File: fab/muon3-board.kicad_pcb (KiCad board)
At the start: 4 copper layers, 160 x 120 mm, 106 parts

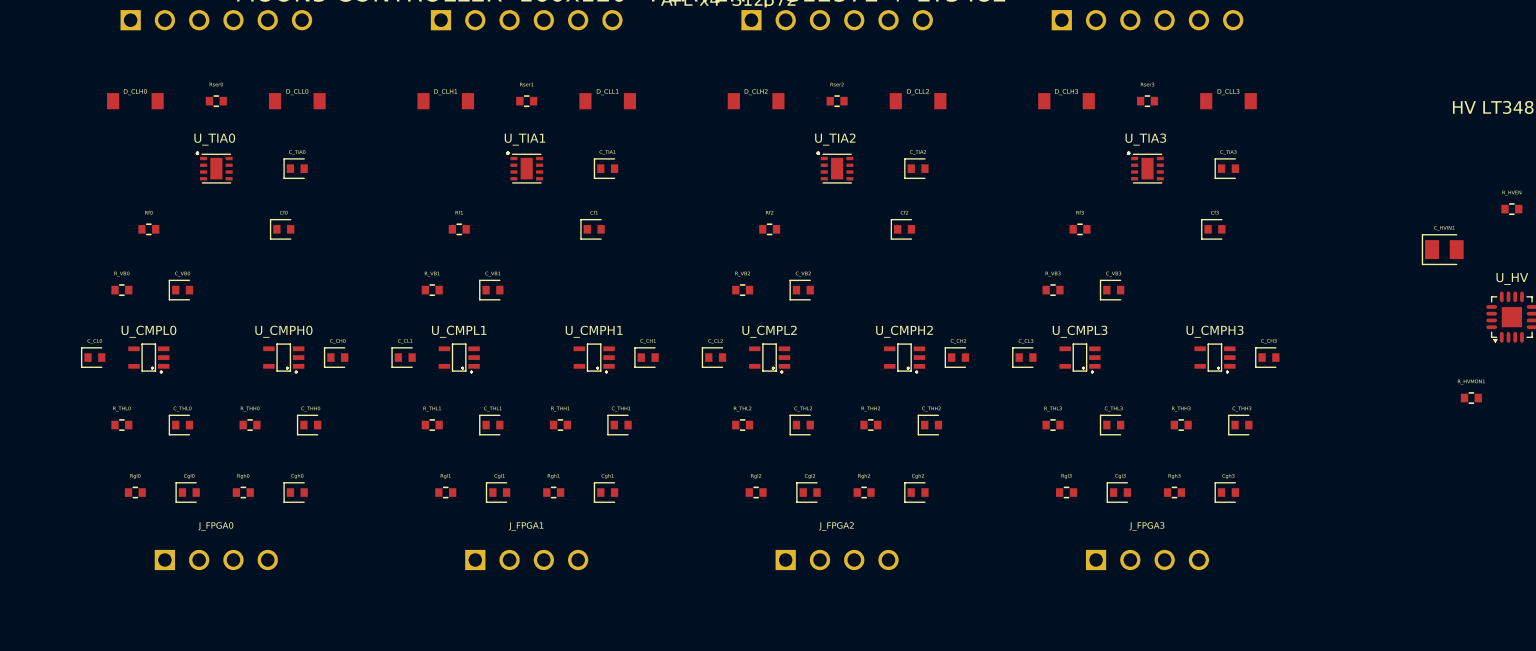
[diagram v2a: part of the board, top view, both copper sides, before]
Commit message: board: datasheet-driven AFE/HV placement (RF/noise/high-speed)
Optimize the placed front-end from vendor layout guidance.

OPA858 TIA (TI SLOS879):
- 10 Ω series R moved directly to the IN− pin (damp bond-wire/stray-C
  resonance) instead of up by the connector.
- VS decoupling (C_TIA) tight to VS_POS; Rf/Cf kept on the FB pin (min
  feedback parasitics) and close to FB/IN−.
- No-pour <keepout> under IN−/OUT/FB on top + L2 reference plane to strip
  summing-node parasitic capacitance (one per channel).
- Off-board SiPM (50 cm cable, fixed) → minimize the on-board connector→
  TIA path; cable modeled in cable_50cm.cir.

TLV3601: VCC decoupling tightened to the pin.

LT3482 HV (ADI 3482fa):
- Add mandatory 20 Ω series R at the APD pin (prevents APD-pin ring-below-
  ground damage on a short).

RF (nRF9151): guidance recorded for when the module is placed — 50 Ω U.FL
edge-launch direct to ANT (single shared LTE+GNSS, no matching), RF trace
on L2 with GND keepout, antenna keepout cylinder.

DRC-clean, zero overlaps. LAYOUT.md updated with the datasheet rationale.

Co-Authored-By: Claude Opus 4.8 <noreply@anthropic.com>
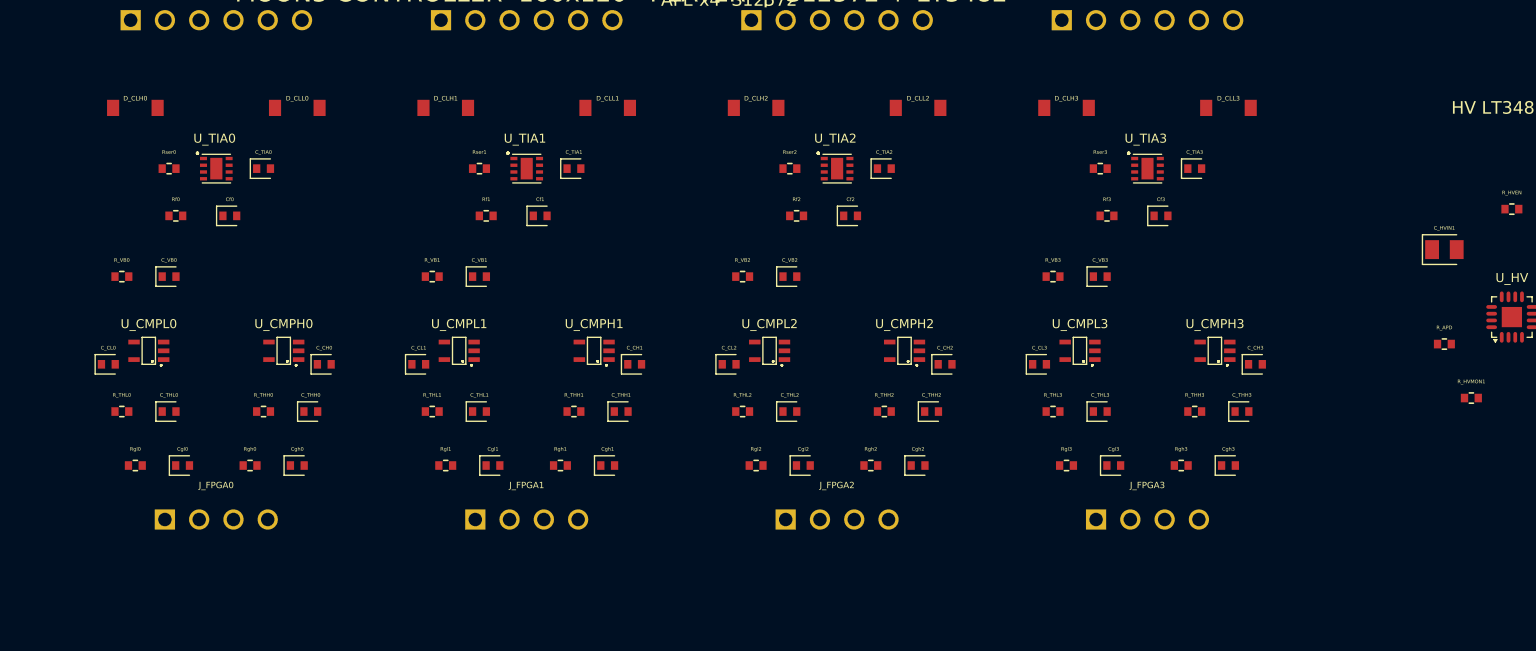
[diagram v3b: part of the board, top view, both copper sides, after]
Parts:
- added R_APD: 20Ω, tscircuit:resistor_res0402, F.Cu at (161.0, 70.0)
- moved Rser0 6.10 mm to (66.5, 57.0)
- moved Rser1 6.10 mm to (89.5, 57.0)
- moved Rser2 6.10 mm to (112.5, 57.0)
- moved Rser3 6.10 mm to (135.5, 57.0)
- moved Cf0 4.12 mm to (71.0, 60.5)
- moved Cf1 4.12 mm to (94.0, 60.5)
- moved Cf2 4.12 mm to (117.0, 60.5)
- moved Cf3 4.12 mm to (140.0, 60.5)
- moved J_FPGA0 3.00 mm to (70.0, 83.0)
- moved J_FPGA1 3.00 mm to (93.0, 83.0)
- moved J_FPGA2 3.00 mm to (116.0, 83.0)
- moved J_FPGA3 3.00 mm to (139.0, 83.0)
- moved C_TIA0 2.50 mm to (73.5, 57.0)
- moved C_TIA1 2.50 mm to (96.5, 57.0)
- moved C_TIA2 2.50 mm to (119.5, 57.0)
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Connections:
- U_HV pad 2: HV_BIAS -> HV_APD

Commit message: board: complete decoupling + rail reservoirs for placed ICs
Add the required passives for the currently-placed subsystems (AFE x4,
HV); per-IC passives for the not-yet-placed digital/TEC/power ICs go in
with those ICs (their pins define the nets).

- OPA858: add per-channel 2.2uF local bulk (C_TIAB) alongside the 0.1uF
  at VS+ (TI SLOS879 layout: 0.1uF + 2.2uF).
- board/rails.tsx: distributed bulk reservoirs on the rails the placed
  parts draw from — VANA 5V (2x10uF+100nF, feeds 4x OPA858), VDIG 3.3V
  (2x10uF+100nF, feeds 8x TLV3601), V12 (22uF+10uF+100nF, feeds LT3482
  and later TEC/fans) — placed at the DIGITAL-zone distribution point.

Already present and audited: TLV3601 0.1uF per comparator; LT3482 input
10uF+100nF, HV_EN pull-up, APD 20 ohm, HV_MON divider.

Deferred (with their ICs): nRF9151/iCE40/RP2040/flash/DAC/ADC/BME280/
CH224K/DRV8873 per-pin decoupling; I2C/reset/boot/config pull-ups;
regulator in/out caps; V1V2 core reservoir.

116 components (41 caps), DRC-clean, zero overlaps.

Co-Authored-By: Claude Opus 4.8 <noreply@anthropic.com>
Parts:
- added C_TIAB0: 2.2uF, tscircuit:capacitor_0603, F.Cu at (76.0, 59.0)
- added C_TIAB1: 2.2uF, tscircuit:capacitor_0603, F.Cu at (99.0, 59.0)
- added C_TIAB2: 2.2uF, tscircuit:capacitor_0603, F.Cu at (122.0, 59.0)
- added C_TIAB3: 2.2uF, tscircuit:capacitor_0603, F.Cu at (145.0, 59.0)
- added C_V12_1: 22uF, tscircuit:capacitor_1206, F.Cu at (114.0, 98.0)
- added C_V12_2: 10uF, tscircuit:capacitor_0805, F.Cu at (118.0, 98.0)
- added C_V12_3: 100nF, tscircuit:capacitor_0402, F.Cu at (121.5, 98.0)
- added C_VANA1: 10uF, tscircuit:capacitor_0805, F.Cu at (58.0, 96.0)
- added C_VANA2: 10uF, tscircuit:capacitor_0805, F.Cu at (62.0, 96.0)
- added C_VANA3: 100nF, tscircuit:capacitor_0402, F.Cu at (65.5, 96.0)
- added C_VDIG1: 10uF, tscircuit:capacitor_0805, F.Cu at (58.0, 101.0)
- added C_VDIG2: 10uF, tscircuit:capacitor_0805, F.Cu at (62.0, 101.0)
- added C_VDIG3: 100nF, tscircuit:capacitor_0402, F.Cu at (65.5, 101.0)

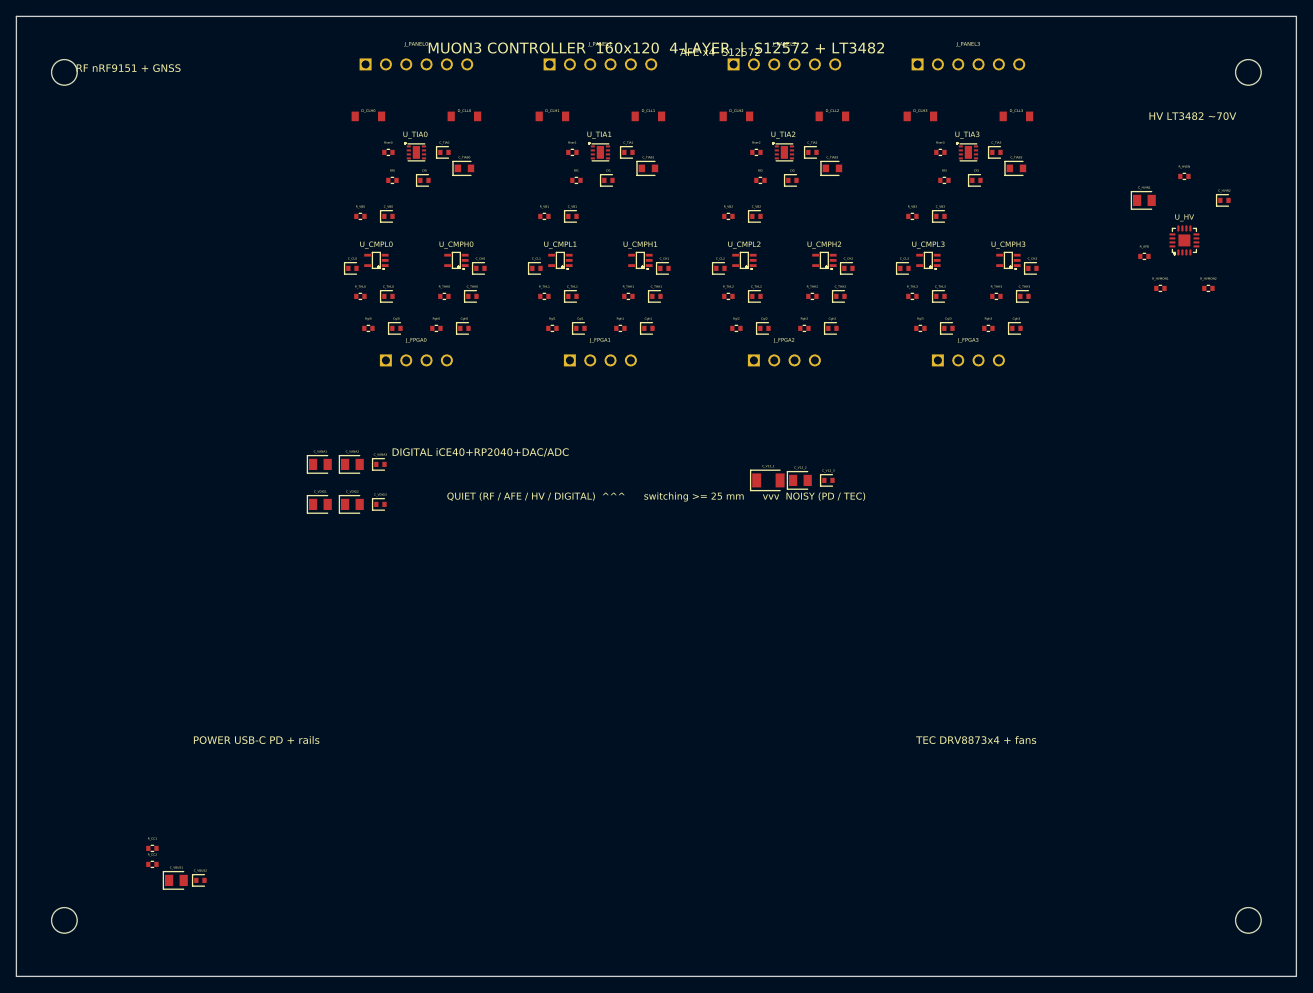
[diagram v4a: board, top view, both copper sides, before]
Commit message: board: populate POWER + RF, board now fully placed (230 components)
- power.tsx: USB-C receptacle (bottom edge, clear of corner hole) -> CH224K
  PD sink (CC pull-downs, CFG code stub for 12V, VDD decoupling, PG pull-up)
  -> TPS62933 3.3V buck with full network (in/out caps, 4.7uH inductor,
  BST/SS/RT, FB divider for 3.3V, EN pull-up).
- rf.tsx: nRF9151-LACA placed with VDD/VIO/VDD_GPIO, DEC0 cap, reset/enable
  pull-ups, supply decoupling; ANT -> U.FL edge-launch (single shared
  LTE+GNSS, 50 ohm, no matching, per Nordic). Import aliased (lowercase
  export name reads as an intrinsic JSX element otherwise).

Whole board: RF | AFE x4 | HV over DIGITAL / POWER / TEC — 230 placements,
49 BOM line items, DRC-clean, zero overlaps.

Flagged for datasheet/routing passes: CH224K 12V CFG code, USB-C A/B pin
map, buck L/FB/RT values, nRF9151 full GND stitch + RF trace, DAC80508 BGA
ball map, LT3482 boost network, VANA/V1V2/VCORE regulators, SIM connector,
and all inter-IC signal buses + routing. README status updated.

Co-Authored-By: Claude Opus 4.8 <noreply@anthropic.com>
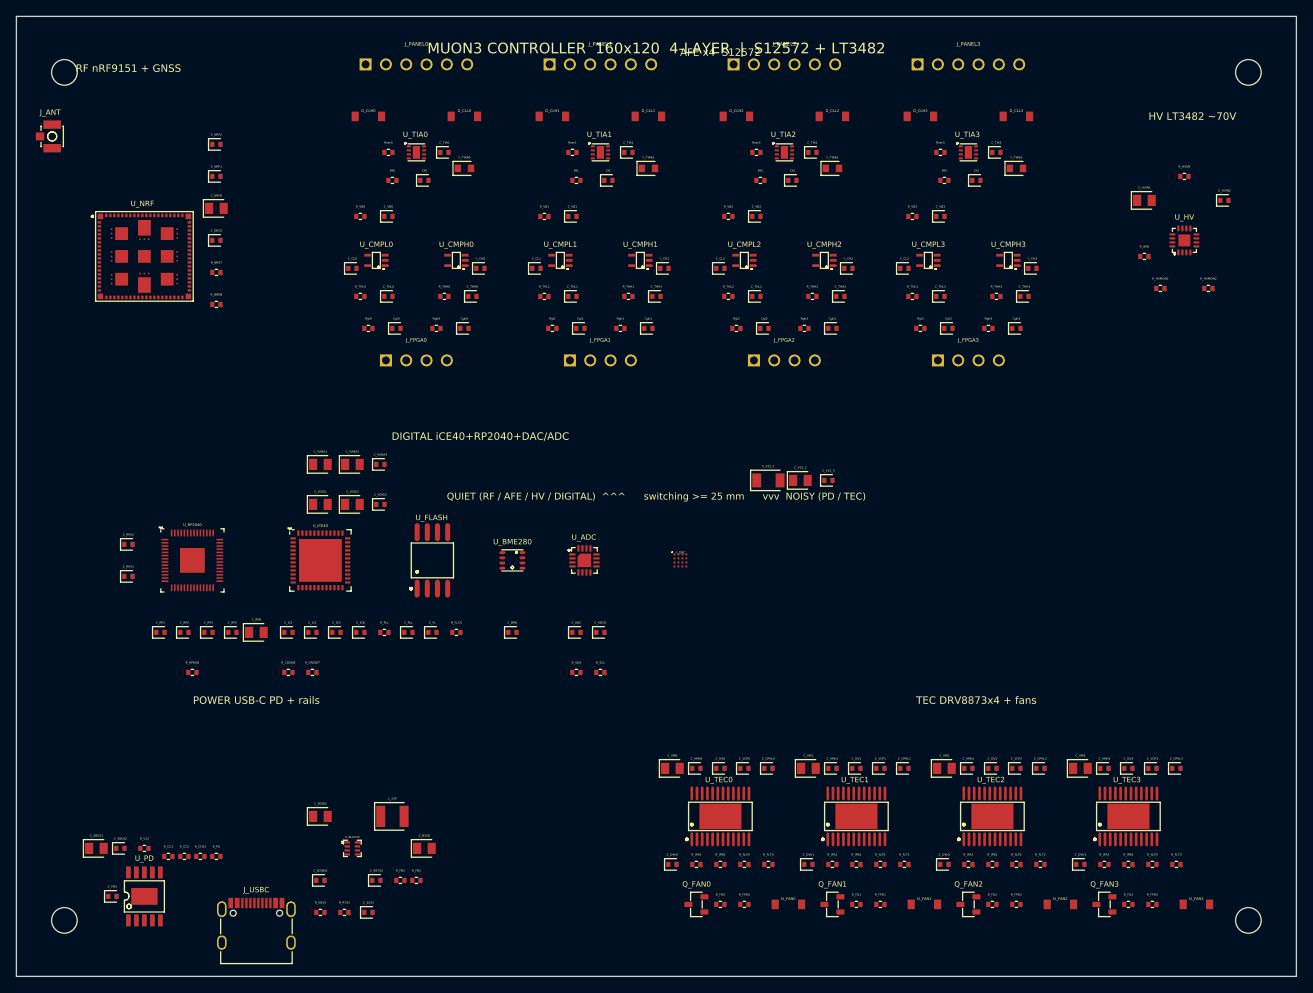
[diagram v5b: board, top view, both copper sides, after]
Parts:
- added C_ADC: 100nF, tscircuit:capacitor_0402, F.Cu at (90.0, 117.0)
- added C_ADCD: 1uF, tscircuit:capacitor_0402, F.Cu at (93.0, 117.0)
- added C_B33IN: 10uF, tscircuit:capacitor_0805, F.Cu at (58.0, 140.0)
- added C_B33IN2: 100nF, tscircuit:capacitor_0402, F.Cu at (58.0, 148.0)
- added C_B33O: 22uF, tscircuit:capacitor_0805, F.Cu at (71.0, 144.0)
- added C_BME: 100nF, tscircuit:capacitor_0402, F.Cu at (82.0, 117.0)
- added C_BST33: 100nF, tscircuit:capacitor_0402, F.Cu at (65.0, 148.0)
- added C_CPHL0: 47nF, tscircuit:capacitor_0402, F.Cu at (114.0, 134.0)
- added C_CPHL1: 47nF, tscircuit:capacitor_0402, F.Cu at (131.0, 134.0)
- added C_CPHL2: 47nF, tscircuit:capacitor_0402, F.Cu at (148.0, 134.0)
- added C_CPHL3: 47nF, tscircuit:capacitor_0402, F.Cu at (165.0, 134.0)
- added C_DEC0: 100nF, tscircuit:capacitor_0402, F.Cu at (45.0, 68.0)
- added C_DV0: 1uF, tscircuit:capacitor_0402, F.Cu at (108.0, 134.0)
- added C_DV1: 1uF, tscircuit:capacitor_0402, F.Cu at (125.0, 134.0)
- added C_DV2: 1uF, tscircuit:capacitor_0402, F.Cu at (142.0, 134.0)
- added C_DV3: 1uF, tscircuit:capacitor_0402, F.Cu at (159.0, 134.0)
- added C_DVh0: 100nF, tscircuit:capacitor_0402, F.Cu at (102.0, 146.0)
- added C_DVh1: 100nF, tscircuit:capacitor_0402, F.Cu at (119.0, 146.0)
- added C_DVh2: 100nF, tscircuit:capacitor_0402, F.Cu at (136.0, 146.0)
- added C_DVh3: 100nF, tscircuit:capacitor_0402, F.Cu at (153.0, 146.0)
- added C_FL: 100nF, tscircuit:capacitor_0402, F.Cu at (72.0, 117.0)
- added C_IC1: 100nF, tscircuit:capacitor_0402, F.Cu at (54.0, 117.0)
- added C_IC2: 100nF, tscircuit:capacitor_0402, F.Cu at (57.0, 117.0)
- added C_IC3: 100nF, tscircuit:capacitor_0402, F.Cu at (60.0, 117.0)
- added C_ICB: 1uF, tscircuit:capacitor_0402, F.Cu at (63.0, 117.0)
- added C_NRF1: 100nF, tscircuit:capacitor_0402, F.Cu at (45.0, 60.0)
- added C_NRF2: 100nF, tscircuit:capacitor_0402, F.Cu at (45.0, 56.0)
- added C_NRFB: 4.7uF, tscircuit:capacitor_0805, F.Cu at (45.0, 64.0)
- added C_PDV: 100nF, tscircuit:capacitor_0402, F.Cu at (32.0, 150.0)
- added C_PLL: 100nF, tscircuit:capacitor_0402, F.Cu at (69.0, 117.0)
- added C_RP1: 100nF, tscircuit:capacitor_0402, F.Cu at (38.0, 117.0)
- added C_RP2: 100nF, tscircuit:capacitor_0402, F.Cu at (41.0, 117.0)
- added C_RP3: 100nF, tscircuit:capacitor_0402, F.Cu at (44.0, 117.0)
- added C_RPB: 10uF, tscircuit:capacitor_0805, F.Cu at (50.0, 117.0)
- added C_RPV: 1uF, tscircuit:capacitor_0402, F.Cu at (47.0, 117.0)
- added C_RPX1: 18pF, tscircuit:capacitor_0402, F.Cu at (34.0, 110.0)
- added C_RPX2: 18pF, tscircuit:capacitor_0402, F.Cu at (34.0, 106.0)
- added C_SS33: 10nF, tscircuit:capacitor_0402, F.Cu at (64.0, 152.0)
- added C_VCP0: 1uF, tscircuit:capacitor_0402, F.Cu at (111.0, 134.0)
- added C_VCP1: 1uF, tscircuit:capacitor_0402, F.Cu at (128.0, 134.0)
- added C_VCP2: 1uF, tscircuit:capacitor_0402, F.Cu at (145.0, 134.0)
- added C_VCP3: 1uF, tscircuit:capacitor_0402, F.Cu at (162.0, 134.0)
- added C_VM0: 10uF, tscircuit:capacitor_0805, F.Cu at (102.0, 134.0)
- added C_VM1: 10uF, tscircuit:capacitor_0805, F.Cu at (119.0, 134.0)
- added C_VM2: 10uF, tscircuit:capacitor_0805, F.Cu at (136.0, 134.0)
- added C_VM3: 10uF, tscircuit:capacitor_0805, F.Cu at (153.0, 134.0)
- added C_VMh0: 100nF, tscircuit:capacitor_0402, F.Cu at (105.0, 134.0)
- added C_VMh1: 100nF, tscircuit:capacitor_0402, F.Cu at (122.0, 134.0)
- added C_VMh2: 100nF, tscircuit:capacitor_0402, F.Cu at (139.0, 134.0)
- added C_VMh3: 100nF, tscircuit:capacitor_0402, F.Cu at (156.0, 134.0)
- added D_FAN0: D, tscircuit:diode_sod123, F.Cu at (116.5, 151.0)
- added D_FAN1: D, tscircuit:diode_sod123, F.Cu at (133.5, 151.0)
- added D_FAN2: D, tscircuit:diode_sod123, F.Cu at (150.5, 151.0)
- added D_FAN3: D, tscircuit:diode_sod123, F.Cu at (167.5, 151.0)
- added J_ANT: BWU_FL_IPEX1, tscircuit:BWU_FL_IPEX1, F.Cu at (24.0, 55.0)
- added J_USBC: TYPE_C_31_M_12, tscircuit:TYPE_C_31_M_12, F.Cu at (50.0, 153.4)
- added L_33V: 4.7µH, tscircuit:inductor_1210, F.Cu at (67.0, 140.0)
- added Q_FAN0: AO3400A, tscircuit:AO3400A, F.Cu at (105.0, 151.0)
- added Q_FAN1: AO3400A, tscircuit:AO3400A, F.Cu at (122.0, 151.0)
- added Q_FAN2: AO3400A, tscircuit:AO3400A, F.Cu at (139.0, 151.0)
- added Q_FAN3: AO3400A, tscircuit:AO3400A, F.Cu at (156.0, 151.0)
- added R_CDONE: 10kΩ, tscircuit:resistor_res0402, F.Cu at (54.0, 122.0)
- added R_CFG2: 6.8kΩ, tscircuit:resistor_res0402, F.Cu at (43.0, 145.0)
- added R_CRESET: 10kΩ, tscircuit:resistor_res0402, F.Cu at (57.0, 122.0)
- added R_EN33: 100kΩ, tscircuit:resistor_res0402, F.Cu at (58.0, 152.0)
- added R_FB1: 100kΩ, tscircuit:resistor_res0402, F.Cu at (68.0, 148.0)
- added R_FB2: 32kΩ, tscircuit:resistor_res0402, F.Cu at (70.0, 148.0)
- added R_FG0: 100Ω, tscircuit:resistor_res0402, F.Cu at (108.0, 151.0)
- added R_FG1: 100Ω, tscircuit:resistor_res0402, F.Cu at (125.0, 151.0)
- added R_FG2: 100Ω, tscircuit:resistor_res0402, F.Cu at (142.0, 151.0)
- added R_FG3: 100Ω, tscircuit:resistor_res0402, F.Cu at (159.0, 151.0)
- added R_FLCS: 10kΩ, tscircuit:resistor_res0402, F.Cu at (75.0, 117.0)
- added R_FLT0: 47kΩ, tscircuit:resistor_res0402, F.Cu at (114.0, 146.0)
- added R_FLT1: 47kΩ, tscircuit:resistor_res0402, F.Cu at (131.0, 146.0)
- added R_FLT2: 47kΩ, tscircuit:resistor_res0402, F.Cu at (148.0, 146.0)
- added R_FLT3: 47kΩ, tscircuit:resistor_res0402, F.Cu at (165.0, 146.0)
- added R_FPD0: 10kΩ, tscircuit:resistor_res0402, F.Cu at (111.0, 151.0)
- added R_FPD1: 10kΩ, tscircuit:resistor_res0402, F.Cu at (128.0, 151.0)
- added R_FPD2: 10kΩ, tscircuit:resistor_res0402, F.Cu at (145.0, 151.0)
- added R_FPD3: 10kΩ, tscircuit:resistor_res0402, F.Cu at (162.0, 151.0)
- added R_IPA0: 1.5kΩ, tscircuit:resistor_res0402, F.Cu at (105.0, 146.0)
- added R_IPA1: 1.5kΩ, tscircuit:resistor_res0402, F.Cu at (122.0, 146.0)
- added R_IPA2: 1.5kΩ, tscircuit:resistor_res0402, F.Cu at (139.0, 146.0)
- added R_IPA3: 1.5kΩ, tscircuit:resistor_res0402, F.Cu at (156.0, 146.0)
- added R_IPB0: 1.5kΩ, tscircuit:resistor_res0402, F.Cu at (108.0, 146.0)
- added R_IPB1: 1.5kΩ, tscircuit:resistor_res0402, F.Cu at (125.0, 146.0)
- added R_IPB2: 1.5kΩ, tscircuit:resistor_res0402, F.Cu at (142.0, 146.0)
- added R_IPB3: 1.5kΩ, tscircuit:resistor_res0402, F.Cu at (159.0, 146.0)
- added R_NREN: 100kΩ, tscircuit:resistor_res0402, F.Cu at (45.0, 76.0)
- added R_NRST: 10kΩ, tscircuit:resistor_res0402, F.Cu at (45.0, 72.0)
- added R_PG: 10kΩ, tscircuit:resistor_res0402, F.Cu at (45.0, 145.0)
- added R_PLL: 100Ω, tscircuit:resistor_res0402, F.Cu at (66.0, 117.0)
- added R_RPRUN: 10kΩ, tscircuit:resistor_res0402, F.Cu at (42.0, 122.0)
- added R_RT33: 100kΩ, tscircuit:resistor_res0402, F.Cu at (61.0, 152.0)
- added R_SCL: 4.7kΩ, tscircuit:resistor_res0402, F.Cu at (93.0, 122.0)
- added R_SDA: 4.7kΩ, tscircuit:resistor_res0402, F.Cu at (90.0, 122.0)
- added R_SLP0: 100kΩ, tscircuit:resistor_res0402, F.Cu at (111.0, 146.0)
- added R_SLP1: 100kΩ, tscircuit:resistor_res0402, F.Cu at (128.0, 146.0)
- added R_SLP2: 100kΩ, tscircuit:resistor_res0402, F.Cu at (145.0, 146.0)
- added R_SLP3: 100kΩ, tscircuit:resistor_res0402, F.Cu at (162.0, 146.0)
- added R_V12: 0Ω, tscircuit:resistor_res0402, F.Cu at (36.0, 144.0)
- added U_ADC: ADS7128IRTER, tscircuit:ADS7128IRTER, F.Cu at (91.0, 108.0)
- added U_BME280: BME280, tscircuit:BME280, F.Cu at (82.0, 108.0)
- added U_BUCK33: TPS62933DRLR, tscircuit:TPS62933DRLR, F.Cu at (62.0, 144.0)
- added U_DAC: DAC80508ZYZFR, tscircuit:DAC80508ZYZFR, F.Cu at (103.0, 108.0)
- added U_FLASH: W25Q128JVSIQ, tscircuit:W25Q128JVSIQ, F.Cu at (72.0, 108.0)
- added U_ICE40: ICE40UP5K_SG48I, tscircuit:ICE40UP5K_SG48I, F.Cu at (58.0, 108.0)
- added U_NRF: nRF9151_LACA_R7, tscircuit:nRF9151_LACA_R7, F.Cu at (36.0, 70.0)
- added U_PD: CH224K, tscircuit:CH224K, F.Cu at (36.0, 150.0)
- added U_RP2040: RP2040, tscircuit:RP2040, F.Cu at (42.0, 108.0)
- added U_TEC0: DRV8873HPWPR, tscircuit:DRV8873HPWPR, F.Cu at (108.0, 140.0)
- added U_TEC1: DRV8873HPWPR, tscircuit:DRV8873HPWPR, F.Cu at (125.0, 140.0)
- added U_TEC2: DRV8873HPWPR, tscircuit:DRV8873HPWPR, F.Cu at (142.0, 140.0)
- added U_TEC3: DRV8873HPWPR, tscircuit:DRV8873HPWPR, F.Cu at (159.0, 140.0)
- moved C_VBUS1 10.8 mm to (30.0, 144.0)
- moved C_VBUS2 10.8 mm to (33.0, 144.0)
- moved R_CC2 4.12 mm to (41.0, 145.0)
- moved R_CC1 2.24 mm to (39.0, 145.0)
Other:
- board text added: "U_DAC (BGA): wire VDD/GND/REF/SPI from datasheet ball map"

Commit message: board: swap DAC to non-BGA DAC80508MRTER (WQFN-16) and wire it
Checked JLCPCB: the BGA DAC80508ZYZFR (grid-only balls, unwireable) has a
non-BGA sibling. DAC80508MRTER — 16-bit, 8-ch, SPI, WQFN-16-EP(3x3),
C2679529, SMT/Standard PCBA — matches the freeze spec with functional pins.
Live stock is low (11 in stock, order qty 10, ~$20); the 14-bit
DAC70508MRTER (C2679508) has only 7 — reserve stock early or qualify at
order time.

- Replace the placed BGA with two DAC80508MRTER (16 outputs per freeze),
  fully wired: VDD on 5 V analog, VIO on 3.3 V SPI logic, GND/EP to GND,
  internal 2.5 V reference (REF 1uF cap), CS/SCLK/SDI on the SPI bus, and
  OUT0-7 broken out to per-DAC nets; VDD/VIO/REF decoupling each.
- Drop the BGA and the 60508/70508 scratch imports.

237 placements, DRC-clean. OUT->AFE-threshold/HV-trim/TEC-setpoint mapping
is part of the signal-bus pass.

Co-Authored-By: Claude Opus 4.8 <noreply@anthropic.com>
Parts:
- removed U_DAC: DAC80508ZYZFR, tscircuit:DAC80508ZYZFR
- added C_DAC1IO: 100nF, tscircuit:capacitor_0402, F.Cu at (104.0, 117.0)
- added C_DAC1R: 1uF, tscircuit:capacitor_0402, F.Cu at (100.0, 117.0)
- added C_DAC1V: 100nF, tscircuit:capacitor_0402, F.Cu at (102.0, 117.0)
- added C_DAC2IO: 100nF, tscircuit:capacitor_0402, F.Cu at (115.0, 117.0)
- added C_DAC2R: 1uF, tscircuit:capacitor_0402, F.Cu at (111.0, 117.0)
- added C_DAC2V: 100nF, tscircuit:capacitor_0402, F.Cu at (113.0, 117.0)
- added U_DAC1: DAC80508MRTER, tscircuit:DAC80508MRTER, F.Cu at (102.0, 108.0)
- added U_DAC2: DAC80508MRTER, tscircuit:DAC80508MRTER, F.Cu at (113.0, 108.0)
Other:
- board text removed: "U_DAC (BGA): wire VDD/GND/REF/SPI from datasheet ball map"
